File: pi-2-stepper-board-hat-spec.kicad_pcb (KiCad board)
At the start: 2 copper layers, 65 x 56 mm, 38 parts, among them CON1 DC12v, P1 Servo, P10 BK_FEED_BYPASS, P2 Endstop1, P3 Endstop2, P4 Stepper1, P5 Stepper2, P6 COM, P7 Aux1 (SPI), P8 Aux2 (I2C)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

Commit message: Added version number v1.0b
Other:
- board text added: "Copyright Mark Benson 2016 License: CC-BY 3.0 No Warranty Implied or given. Use at own risk!"
- board text added: "v1.0b"
- board text removed: "Copyright Mark Benson 2016 License: CC-BY 3.0"
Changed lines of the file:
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@@
     (links 133)
     (no_connects 0)
-    (area 76.496999 43.6425 144.767455 100.287501)
+    (area 76.680389 43.916348 141.857801 100.100575)
     (thickness 1.6)
-    (drawings 30)
+    (drawings 32)
     (tracks 719)
     (zones 0)
@@
     (fp_line (start 0.35052 0.89916) (end 0.7493 1.89992) (layer F.SilkS) (width 0.15))
   )
+  (gr_text v1.0b (at 131.572 92.9005) (layer B.SilkS)
+    (effects (font (size 1.5 1.5) (thickness 0.3)) (justify mirror))
+  )
+  (gr_text v1.0b (at 131.6355 92.9005) (layer F.SilkS)
+    (effects (font (size 1.5 1.5) (thickness 0.3)))
+  )
   (gr_text github.com/markjb/pi-2-stepper-board (at 126.492 79.502 90) (layer B.SilkS)
     (effects (font (size 1 1) (thickness 0.15)) (justify mirror))
@@
     (effects (font (size 1 1) (thickness 0.15)) (justify mirror))
   )
-  (gr_text "Copyright\nMark Benson\n2016\nLicense:\nCC-BY 3.0\n" (at 94.361 74.041) (layer B.SilkS)
+  (gr_text "Copyright\nMark Benson\n2016\nLicense:\nCC-BY 3.0\nNo Warranty\nImplied\nor given.\nUse at own\nrisk!" (at 94.361 74.7395) (layer B.SilkS)
     (effects (font (size 1 1) (thickness 0.15)) (justify mirror))
   )

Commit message: Update licence version
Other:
- board text added: "Copyright Mark Benson 2016 License: CC-BY 4.0 No Warranty Implied or given. Use at own risk!"
- board text removed: "Copyright Mark Benson 2016 License: CC-BY 3.0 No Warranty Implied or given. Use at own risk!"
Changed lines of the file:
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@@
     (effects (font (size 1 1) (thickness 0.15)) (justify mirror))
   )
-  (gr_text "Copyright\nMark Benson\n2016\nLicense:\nCC-BY 3.0\nNo Warranty\nImplied\nor given.\nUse at own\nrisk!" (at 94.361 74.7395) (layer B.SilkS)
+  (gr_text "Copyright\nMark Benson\n2016\nLicense:\nCC-BY 4.0\nNo Warranty\nImplied\nor given.\nUse at own\nrisk!" (at 94.361 74.7395) (layer B.SilkS)
     (effects (font (size 1 1) (thickness 0.15)) (justify mirror))
   )

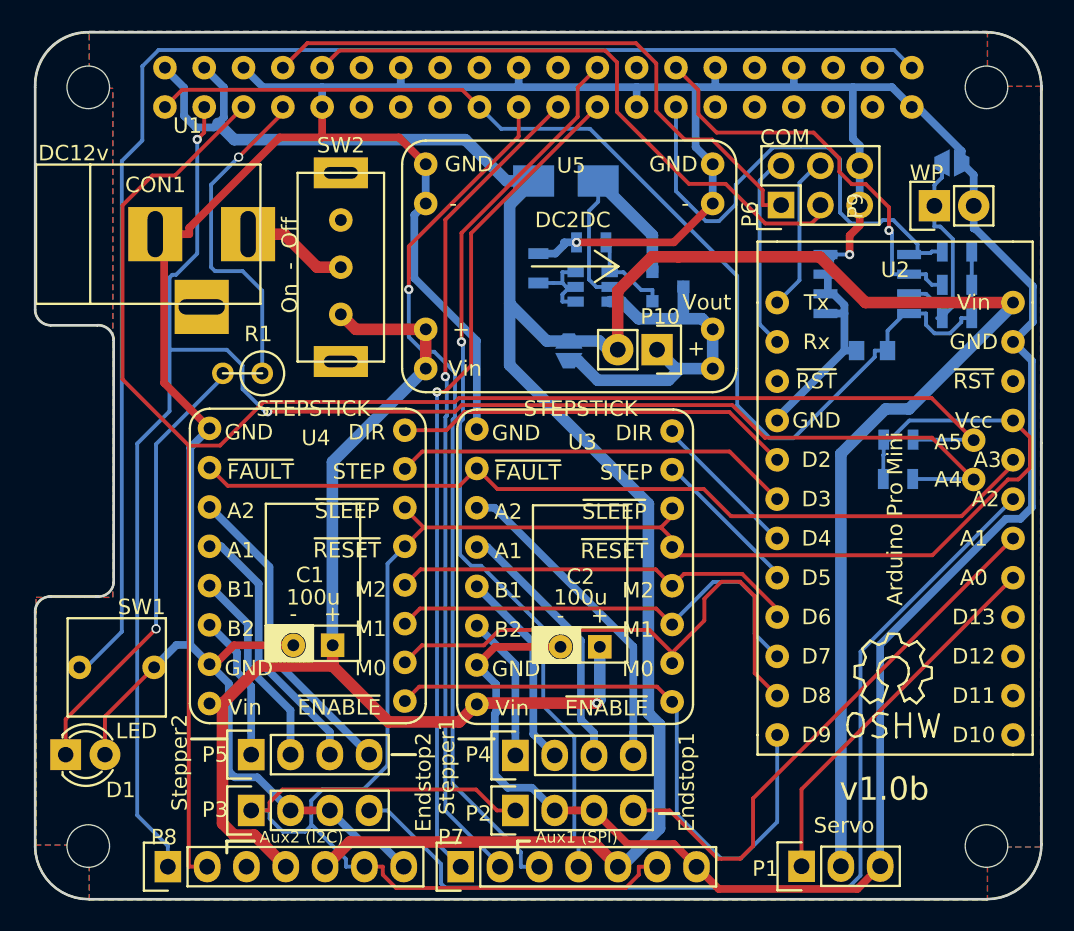
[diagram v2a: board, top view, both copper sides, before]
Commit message: Milestone 1.01b fixes
Swapped com port sides
Replaced LED with Bi-colour LED
Fixed Silkscreen & NPTH plated slot
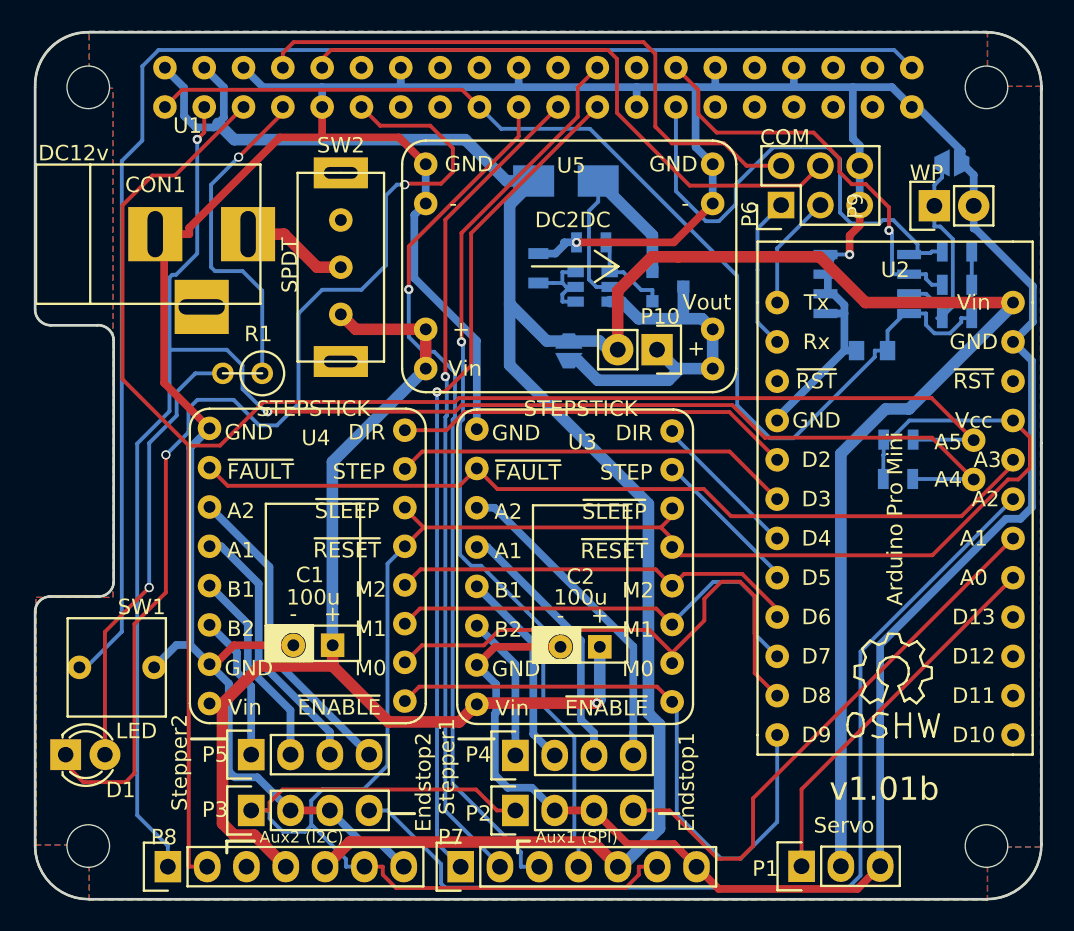
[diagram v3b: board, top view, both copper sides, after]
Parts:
- SW2: value On - Off -> SPDT
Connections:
- net /LED renamed /LEDA
- D1 pad 1: Net-(D1-Pad1) -> /LEDB
- D1 pad 2: GND -> Net-(D1-Pad2)
- P6 pad 1: /PiTx -> /ArdRx
- P6 pad 2: /ArdRx -> /PiTx
- P6 pad 3: /PiRx -> /ArdTx
- P6 pad 4: /ArdTx -> /PiRx
- R1 pad 2: Net-(D1-Pad1) -> Net-(D1-Pad2)
- U1 pad 11: Net-(U1-Pad11) -> /LEDB
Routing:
- net /LEDB: track 0.00 -> 70.2 mm, vias 0 -> 2
- net Net-(D1-Pad2): track 0.00 -> 29.1 mm, vias 0 -> 1
- net Net-(D1-Pad1): track 28.8 -> 0.00 mm, vias 1 -> 0
- net GND: track 310.6 -> 303.7 mm
- net /ArdRx: track 12.7 -> 10.00 mm
- net /ArdTx: track 10.3 -> 8.26 mm
- net /PiTx: track 39.6 -> 40.1 mm
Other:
- board text added: "v1.01b"
- board text removed: "v1.0b"
